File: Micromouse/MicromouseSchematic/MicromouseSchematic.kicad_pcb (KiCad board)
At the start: 2 copper layers, 155.7 x 22.6 mm, 101 parts, among them J1 Conn_01x06_MountingPin, J10 Conn_01x06_MountingPin, J11 Conn_01x07_Pin, J2 Conn_01x06_MountingPin, J3 Conn_01x03_Pin, J4 Conn_01x02_Pin, J5 Conn_01x06_MountingPin, J6 IR_1, J7 IR_2, J8 IR_3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

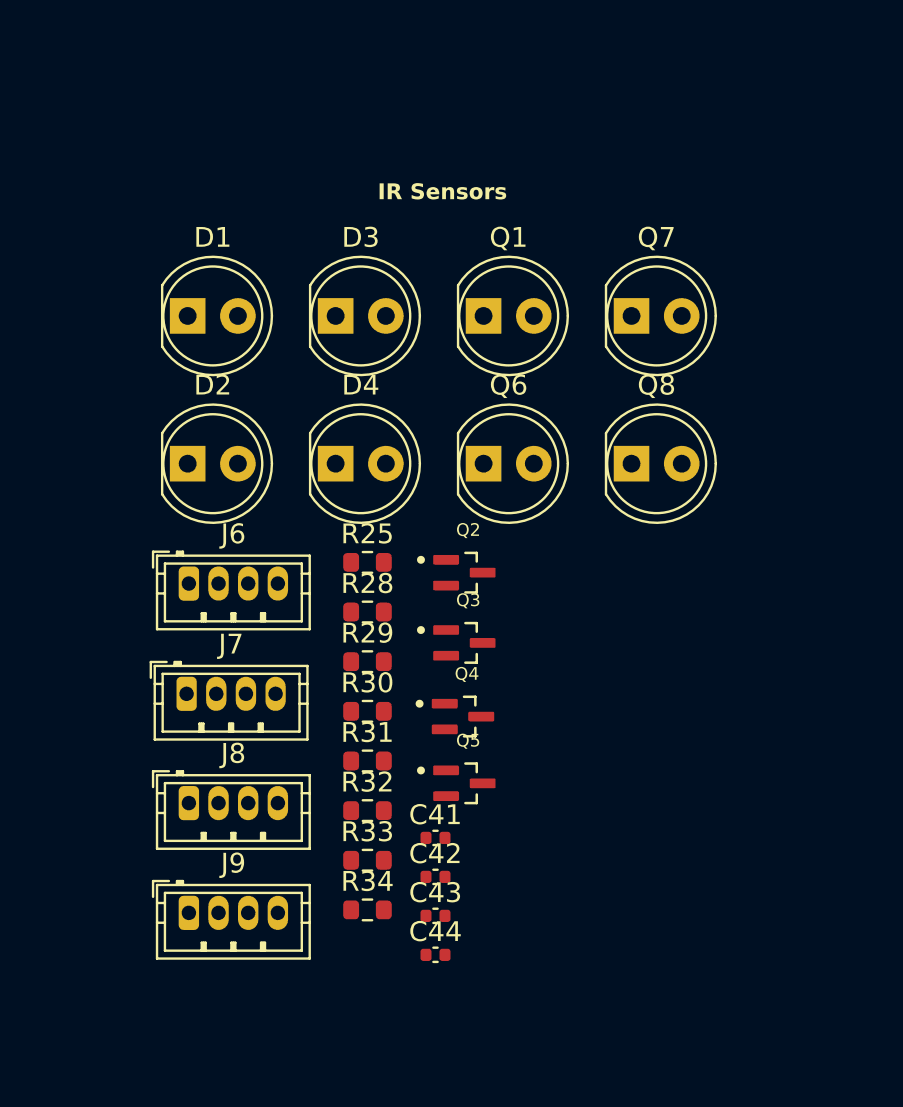
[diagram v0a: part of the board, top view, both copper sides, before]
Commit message: added ir sensors stuff
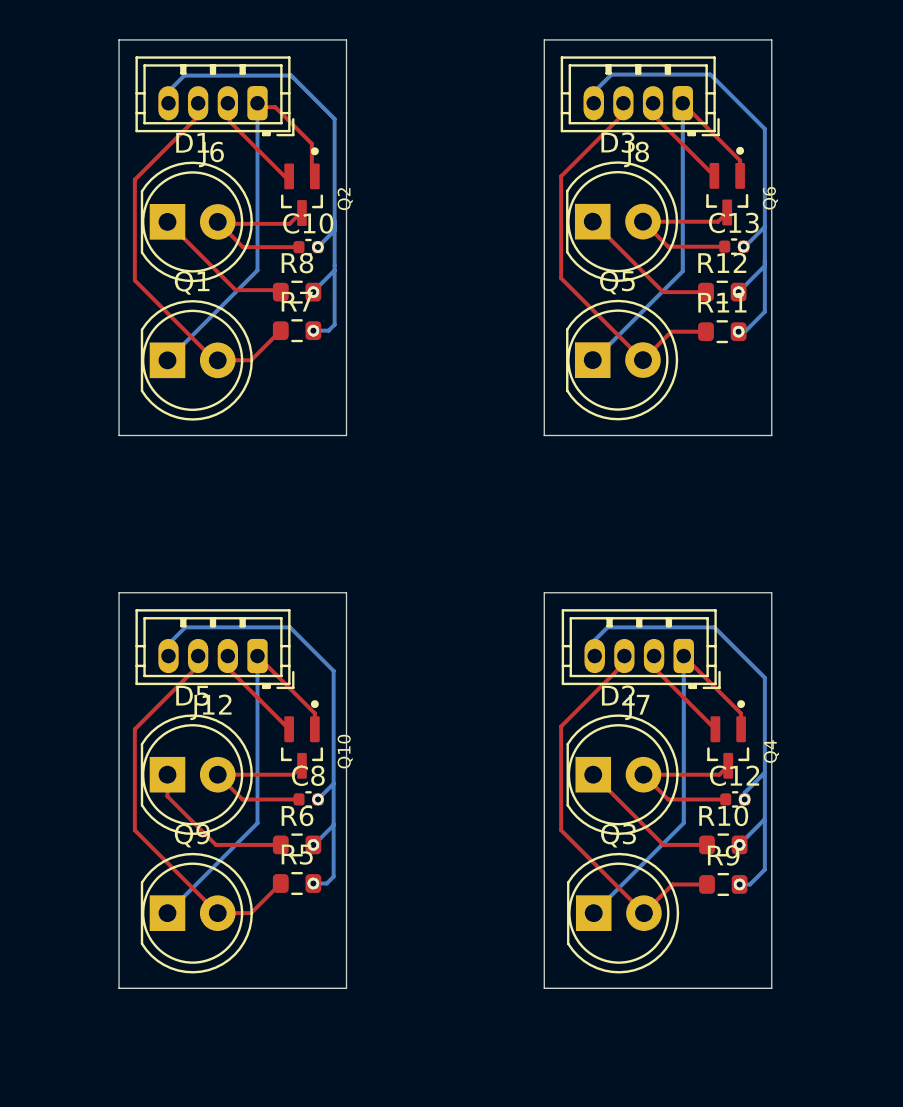
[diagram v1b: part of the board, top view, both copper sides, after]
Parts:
- removed C41, C42, C43, C44: 1uF, Capacitor_SMD:C_0402_1005Metric
- removed D4: SFH4550, LED_THT:LED_D5.0mm_IRGrey
- removed J9: IR_4, Connector_JST:JST_ZH_B4B-ZR_1x04_P1.50mm_Vertical
- removed Q7, Q8: SFH300, LED_THT:LED_D5.0mm_Clear
- removed R25, R29, R31, R33: 10k, Resistor_SMD:R_0603_1608Metric
- removed R28, R30, R32, R34: 100, Resistor_SMD:R_0603_1608Metric
- added C10: 1uF, Capacitor_SMD:C_0402_1005Metric, F.Cu at (123.1, 27.5)
- added C12: 1uF, Capacitor_SMD:C_0402_1005Metric, F.Cu at (144.7, 55.4)
- added C13: 1uF, Capacitor_SMD:C_0402_1005Metric, F.Cu at (144.6, 27.4)
- added C8: 1uF, Capacitor_SMD:C_0402_1005Metric, F.Cu at (123.1, 55.4)
- added D5: SFH4550, LED_THT:LED_D5.0mm_IRGrey, F.Cu at (116.0, 54.1)
- added J12: IR_1, Connector_JST:JST_ZH_B4B-ZR_1x04_P1.50mm_Vertical, F.Cu at (120.5, 48.1)
- added Q10: DMN3065LW-7, MM_DMN3065LW-7:DMN3065LW-7, F.Cu at (122.8, 52.8)
- added Q9: SFH300, LED_THT:LED_D5.0mm_Clear, F.Cu at (116.0, 61.1)
- added R10: 100, Resistor_SMD:R_0603_1608Metric, F.Cu at (144.1, 57.7)
- added R11: 10k, Resistor_SMD:R_0603_1608Metric, F.Cu at (144.0, 31.8)
- added R12: 100, Resistor_SMD:R_0603_1608Metric, F.Cu at (144.0, 29.8)
- added R5: 10k, Resistor_SMD:R_0603_1608Metric, F.Cu at (122.5, 59.6)
- added R6: 100, Resistor_SMD:R_0603_1608Metric, F.Cu at (122.5, 57.7)
- added R7: 10k, Resistor_SMD:R_0603_1608Metric, F.Cu at (122.5, 31.7)
- added R8: 100, Resistor_SMD:R_0603_1608Metric, F.Cu at (122.5, 29.8)
- added R9: 10k, Resistor_SMD:R_0603_1608Metric, F.Cu at (144.1, 59.7)
- J7: value IR_2 -> IR_1
- J8: value IR_3 -> IR_1
- Q3, Q5: value DMN3065LW-7 -> SFH300; footprint MM_DMN3065LW-7:DMN3065LW-7 -> LED_THT:LED_D5.0mm_Clear
- Q6: value SFH300 -> DMN3065LW-7; footprint LED_THT:LED_D5.0mm_Clear -> MM_DMN3065LW-7:DMN3065LW-7
- moved J8 43.3 mm to (142.0, 20.2), turned to 180 degrees
- moved D2 25.8 mm to (137.5, 54.1)
- moved J7 25.2 mm to (142.1, 48.1), turned to 180 degrees
- moved J6 24.5 mm to (120.5, 20.2), turned to 180 degrees
- moved Q5 22.4 mm to (137.4, 33.2)
- moved Q2 20.8 mm to (122.8, 24.8), turned to -90 degrees
- moved Q6 18.4 mm to (144.2, 24.8), turned to -90 degrees
- moved Q1 16.1 mm to (116.0, 33.2)
- moved Q3 15.1 mm to (137.5, 61.1)
- moved D3 13.8 mm to (137.4, 26.2)
- moved Q4 13.5 mm to (144.3, 52.8), turned to -90 degrees
- moved D1 4.86 mm to (116.0, 26.2)
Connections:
- J6 pad 2: IR_POW_1 -> IR_POW_2
- J6 pad 3: IR_REC_1 -> IR_REC_2
- J7 pad 2: IR_POW_2 -> IR_POW_3
- J7 pad 3: IR_REC_2 -> IR_REC_3
- J8 pad 2: IR_POW_3 -> IR_POW_4
- J8 pad 3: IR_REC_3 -> IR_REC_4
- Q1 pad 2: IR_REC_4 -> IR_REC_2
- Q2 pad 2: IR_POW_1 -> IR_POW_2
- Q2 pad 3: Net-(D3-A) -> Net-(D1-A)
- Q3 pad 2: IR_POW_2 -> IR_REC_3
- Q4 pad 3: Net-(D4-A) -> Net-(D2-A)
- Q5 pad 2: IR_POW_4 -> IR_REC_4
- Q6 pad 2: IR_REC_1 -> IR_POW_4
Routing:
- net GND: track 82.5 -> 183.2 mm, vias 0 -> 12
- net +3.3V: track 69.1 -> 148.5 mm
- net IR_REC_2: track 0.00 -> 20.2 mm
- net IR_REC_1: track 0.00 -> 19.9 mm
- net IR_REC_3: track 0.00 -> 19.8 mm
- net IR_REC_4: track 0.00 -> 19.8 mm
- net Net-(D2-A): track 0.00 -> 9.14 mm
- net Net-(D3-A): track 0.00 -> 9.10 mm
- net Net-(D5-A): track 0.00 -> 9.07 mm
- net Net-(D1-A): track 0.00 -> 8.95 mm
- net Net-(D5-K): track 0.00 -> 7.84 mm
- net Net-(D1-K): track 0.00 -> 7.33 mm
- net Net-(D2-K): track 0.00 -> 7.22 mm
- net Net-(D3-K): track 0.00 -> 7.20 mm
- net IR_POW_3: track 0.00 -> 4.98 mm
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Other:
- board size 155.7 x 22.6 mm -> 155.7 x 48 mm
- board text removed: "IR Sensors"

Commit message: Completed motor driver layout
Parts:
- removed C10, C12, C13, C8: 1uF, Capacitor_SMD:C_0402_1005Metric
- removed D5: SFH4550, LED_THT:LED_D5.0mm_IRGrey
- removed Q10: DMN3065LW-7, MM_DMN3065LW-7:DMN3065LW-7
- removed Q9: SFH300, LED_THT:LED_D5.0mm_Clear
- removed R10, R12, R6, R8: 100, Resistor_SMD:R_0603_1608Metric
- removed R11, R5, R7, R9: 10k, Resistor_SMD:R_0603_1608Metric
- added C41: 1uF, Capacitor_SMD:C_0402_1005Metric, F.Cu at (129.5, 57.3)
- added C42: 1uF, Capacitor_SMD:C_0402_1005Metric, F.Cu at (129.5, 59.3)
- added C43: 1uF, Capacitor_SMD:C_0402_1005Metric, F.Cu at (129.5, 61.3)
- added C44: 1uF, Capacitor_SMD:C_0402_1005Metric, F.Cu at (129.5, 63.3)
- added Cin_MD2: 22 μF, Capacitor_SMD:C_0402_1005Metric, F.Cu at (63.4, 107.0)
- added D4: SFH4550, LED_THT:LED_D5.0mm_IRGrey, F.Cu at (124.5, 38.4)
- added J13: Conn_01x10, Connector_JST:JST_ZH_B10B-ZR_1x10_P1.50mm_Vertical, F.Cu at (69.3, 121.4)
- added J9: IR_4, Connector_JST:JST_ZH_B4B-ZR_1x04_P1.50mm_Vertical, F.Cu at (117.0, 61.1)
- added Q7: SFH300, LED_THT:LED_D5.0mm_Clear, F.Cu at (139.4, 31.0)
- added Q8: SFH300, LED_THT:LED_D5.0mm_Clear, F.Cu at (139.4, 38.4)
- added R25: 10k, Resistor_SMD:R_0603_1608Metric, F.Cu at (126.1, 43.4)
- added R28: 100, Resistor_SMD:R_0603_1608Metric, F.Cu at (126.1, 45.9)
- added R29: 10k, Resistor_SMD:R_0603_1608Metric, F.Cu at (126.1, 48.4)
- added R30: 100, Resistor_SMD:R_0603_1608Metric, F.Cu at (126.1, 50.9)
- added R31: 10k, Resistor_SMD:R_0603_1608Metric, F.Cu at (126.1, 53.5)
- added R32: 100, Resistor_SMD:R_0603_1608Metric, F.Cu at (126.1, 56.0)
- added R33: 10k, Resistor_SMD:R_0603_1608Metric, F.Cu at (126.1, 58.5)
- added R34: 100, Resistor_SMD:R_0603_1608Metric, F.Cu at (126.1, 61.0)
- J12: value IR_1 -> Conn_01x10; footprint Connector_JST:JST_ZH_B4B-ZR_1x04_P1.50mm_Vertical -> Connector_JST:JST_ZH_B10B-ZR_1x10_P1.50mm_Vertical
- J7: value IR_1 -> IR_2
- J8: value IR_1 -> IR_3
- Q3, Q5: value SFH300 -> DMN3065LW-7; footprint LED_THT:LED_D5.0mm_Clear -> MM_DMN3065LW-7:DMN3065LW-7
- Q6: value DMN3065LW-7 -> SFH300; footprint MM_DMN3065LW-7:DMN3065LW-7 -> LED_THT:LED_D5.0mm_Clear
- moved J12 68.7 mm to (69.0, 93.6), turned to -90 degrees
- moved J1 45.8 mm to (44.7, 124.4), turned to -90 degrees
- moved R38 43.5 mm to (59.3, 128.9), turned to -90 degrees
- moved J8 43.3 mm to (117.0, 55.6), turned to 0 degrees
- moved R37 43.1 mm to (59.7, 125.9)
- moved R21 40.5 mm to (52.7, 131.1), turned to -90 degrees
- moved C3 37.9 mm to (51.6, 128.6), turned to 180 degrees
- moved Cin_MD1 37.4 mm to (64.3, 134.4), turned to 90 degrees
- moved C1 36.8 mm to (49.4, 131.9), turned to -90 degrees
- moved U7 34.7 mm to (55.1, 127.4), turned to -90 degrees
- moved R41 31.3 mm to (59.7, 123.8)
- moved R42 29.8 mm to (64.7, 122.8), turned to 180 degrees
- moved D2 25.8 mm to (117.0, 38.4)
- moved J7 25.2 mm to (116.9, 50.1), turned to 0 degrees
- moved J6 24.5 mm to (117.0, 44.5), turned to 0 degrees
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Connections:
- J12 pad 2: IR_POW_1 -> NSLEEP_HB_2
- J12 pad 3: IR_REC_1 -> NSLEEP_LDO_2
- J12 pad 4: GND -> MO2_IN1
- J6 pad 2: IR_POW_2 -> IR_POW_1
- J6 pad 3: IR_REC_2 -> IR_REC_1
- J7 pad 2: IR_POW_3 -> IR_POW_2
- J7 pad 3: IR_REC_3 -> IR_REC_2
- J8 pad 2: IR_POW_4 -> IR_POW_3
- J8 pad 3: IR_REC_4 -> IR_REC_3
- Q1 pad 2: IR_REC_2 -> IR_REC_4
- Q2 pad 2: IR_POW_2 -> IR_POW_1
- Q2 pad 3: Net-(D1-A) -> Net-(D3-A)
- Q3 pad 2: IR_REC_3 -> IR_POW_2
- Q4 pad 3: Net-(D2-A) -> Net-(D4-A)
- Q5 pad 2: IR_REC_4 -> IR_POW_4
- Q6 pad 2: IR_POW_4 -> IR_REC_1
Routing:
- net +7.4V: track 30.3 -> 66.3 mm
- net Net-(U11-NSLEEP_HB): track 0.00 -> 32.5 mm, vias 0 -> 4
- net +3.3V: track 148.5 -> 177.6 mm
- net Encoder_B_2: track 0.00 -> 25.6 mm
- net Encoder_B_1: track 0.00 -> 25.6 mm
- net Encoder_A_2: track 0.00 -> 25.2 mm, vias 0 -> 1
- net Encoder_A_1: track 0.00 -> 25.2 mm, vias 0 -> 1
- net MO2_IN2: track 0.00 -> 20.7 mm
- net IR_REC_2: track 20.2 -> 0.00 mm
- net IR_REC_1: track 19.9 -> 0.00 mm
- net IR_REC_3: track 19.8 -> 0.00 mm
- net IR_REC_4: track 19.8 -> 0.00 mm
- net GND: track 183.2 -> 202.9 mm, vias 12 -> 4
- net Net-(J1-Pin_2): track 0.00 -> 14.0 mm, vias 0 -> 1
- net Net-(J2-Pin_2): track 0.00 -> 14.0 mm, vias 0 -> 1
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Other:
- board size 155.7 x 48 mm -> 169.9 x 112.6 mm
- board text added: "Driver 1"
- board text added: "Driver 2"
- board text added: "IR Sensors"
- board text removed: "Motor Drivers"
